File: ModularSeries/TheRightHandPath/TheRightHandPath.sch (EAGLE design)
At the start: 74 parts, among them IC1 ATTINY861_DIP, IC2 SN74HCX38, IC3 SN74HCX38, IC4 LM358_DIP, IC5 TL0X2_DIP

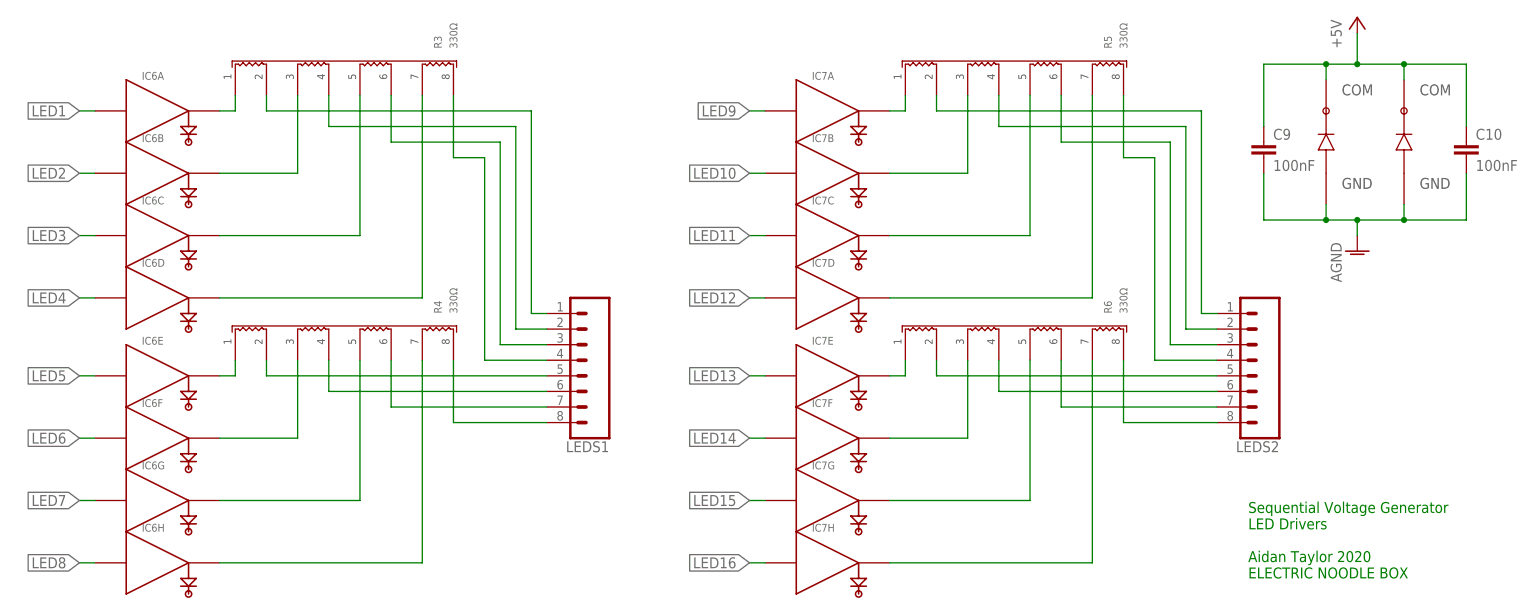
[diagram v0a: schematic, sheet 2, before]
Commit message: Library updated, variants consolidated
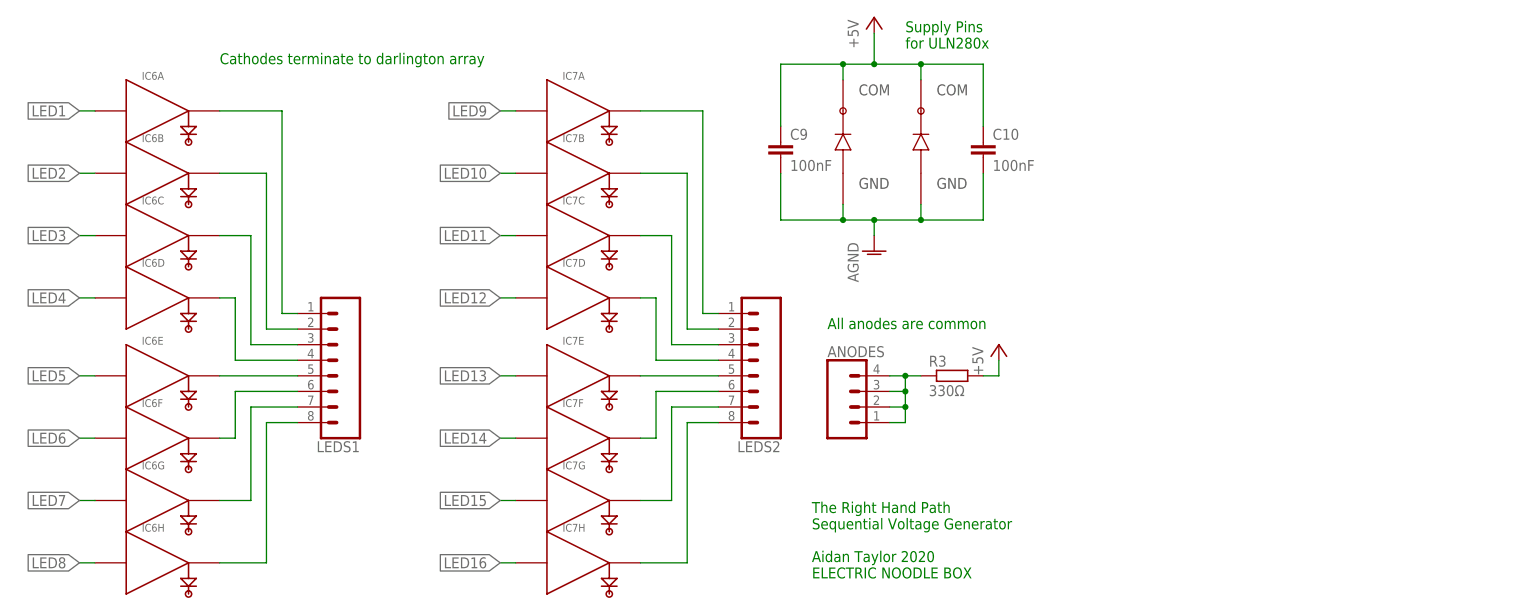
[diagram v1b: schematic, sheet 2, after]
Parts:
- removed CLK_MOD, LENGTH, START: 1XWIREPAD, ElectricNoodleBox:1XWIREPAD
- removed R11, R12, R44, R45, R46, R47: 10K, rcl:R-EU_0207/10
- added ANODES: 4XWIREPAD, ElectricNoodleBox:4XWIREPAD
- added D5: 4V7, diode:ZENER-DIODEDO35Z10
- added GSW, LN_CV, RUNSTOP: 1XWIREPAD, ElectricNoodleBox:1XWIREPAD
- R3: device ElectricNoodleBox:4XISO_RESISTOR_NETWORK_2.54 -> rcl:R-EU_0207/10
- R4, R5: value 330Ω -> 10K; device ElectricNoodleBox:4XISO_RESISTOR_NETWORK_2.54 -> rcl:R-EU_0207/10
- R6: value 330Ω -> 100Ω; device ElectricNoodleBox:4XISO_RESISTOR_NETWORK_2.54 -> rcl:R-EU_0207/10
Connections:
- removed net N$19: LEDS1.5, R4.P$2
- removed net N$21: LEDS1.6, R4.P$4
- removed net N$23: LEDS1.7, R4.P$6
- removed net N$25: LEDS1.8, R4.P$8
- removed net N$27: LEDS2.1, R5.P$2
- removed net N$29: LEDS2.2, R5.P$4
- removed net N$31: LEDS2.3, R5.P$6
- removed net N$33: LEDS2.4, R5.P$8
- removed net N$35: LEDS2.5, R6.P$2
- removed net N$37: LEDS2.6, R6.P$4
- removed net N$39: LEDS2.7, R6.P$6
- removed net N$41: LEDS2.8, R6.P$8
- removed net N$68: IC4B.-IN, R45.2, R46.1, R47.2
- removed net N$69: IC1.20_PA0, IC4B.OUT, R46.2
- removed net N$70: INT_CLK.1, R47.1
- removed net N$72: IC1.7_PB4, LENGTH.1
- removed net N$78: IC4B.+IN, R11.1, R12.2
- removed net N$79: IC1.13_PA5, IC3.1_A
- new net 2V5REF: IC4B.+IN, R40.2
- new net GATEWIDTH: IC1.11_PA7
- net +5V: now also R3.2; no longer IC4A.+IN, R12.1
- net AGND: now also D5.A, R4.1; no longer IC2.5_/G2B, IC3.5_/G2B, R11.2, R44.1
- net N$1: now also IC1.14_PA4; no longer IC1.4_PB3
- net N$10: now also LEDS1.1; no longer R3.P$1
- net N$11: now also IC1.7_PB4, INT_CLK.1; no longer LEDS1.1, R3.P$2
- net N$12: now also LEDS1.2; no longer R3.P$3
- net N$13: now also IC1.12_PA6, IC2.5_/G2B, IC3.5_/G2B; no longer LEDS1.2, R3.P$4
- net N$14: now also LEDS1.3; no longer R3.P$5
- net N$15: now also IC4B.OUT, R5.1, R6.2; no longer LEDS1.3, R3.P$6
- net N$16: now also LEDS1.4; no longer R3.P$7
- net N$17: now also D5.C, IC1.20_PA0, R6.1; no longer LEDS1.4, R3.P$8
- net N$18: now also LEDS1.5; no longer R4.P$1
- net N$2: now also IC3.3_C
- net N$20: now also LEDS1.6; no longer R4.P$3
- net N$22: now also LEDS1.7; no longer R4.P$5
- net N$24: now also LEDS1.8; no longer R4.P$7
- net N$26: now also LEDS2.1; no longer R5.P$1
- net N$28: now also LEDS2.2; no longer R5.P$3
- net N$3: now also IC3.2_B
- net N$30: now also LEDS2.3; no longer R5.P$5
- net N$32: now also LEDS2.4; no longer R5.P$7
- net N$34: now also LEDS2.5; no longer R6.P$1
- net N$36: now also LEDS2.6; no longer R6.P$3
- net N$38: now also LEDS2.7; no longer R6.P$5
- net N$4: now also IC3.1_A
- net N$40: now also LEDS2.8; no longer R6.P$7
- net N$5: now also RUNSTOP.1; no longer START.1
- net N$6: now also GSW.1, IC1.13_PA5; no longer IC1.12_PA6, IC3.2_B
- net N$67: now also IC4B.-IN, R4.2, R5.2; no longer R44.2, R45.1
- net N$7: now also ANODES.1, ANODES.2, ANODES.3, ANODES.4, R3.1; no longer IC1.11_PA7, IC3.3_C
- net N$71: now also LN_CV.1; no longer CLK_MOD.1
- net N$77: now also IC1.4_PB3; no longer IC1.14_PA4
- net SCK: now also IC4A.+IN; no longer R40.2
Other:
- note added: "All anodes are common"
- note added: "Cathodes terminate to darlington array"
- note added: "External clock in"
- note added: "Gate out"
- note added: "ICSP Header"
- note added: "PA4 selects between decoders PA6 enables/disables both"
- note added: "Run/Stop In"
- note added: "Supply Pins for ULN280x"
- note added: "The Right Hand Path Sequential Voltage Generator Aidan Taylor 2020 ELECTRIC NOODLE BOX"
- note added: "The Right Hand Path: Sequential Voltage Generator Aidan Taylor 2020 ELECTRIC NOODLE BOX"
- note removed: "Forwards/Backwards"
- note removed: "Internal clock and modulation"
- note removed: "Sequence clock in"
- note removed: "Sequential Voltage Generator Aidan Taylor 2020 ELECTRIC NOODLE BOX"
- note removed: "Sequential Voltage Generator LED Drivers Aidan Taylor 2020 ELECTRIC NOODLE BOX"
- note removed: "Start/Stop"
- moved on the sheet: 5VT, C10, C9, D2, D4, GATE_OUT, GNDT2, H1, H2, H3, H4, IC4A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
